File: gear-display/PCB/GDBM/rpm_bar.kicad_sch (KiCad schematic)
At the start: 7 parts, among them J4 Con_Screw_1x04_691313510004

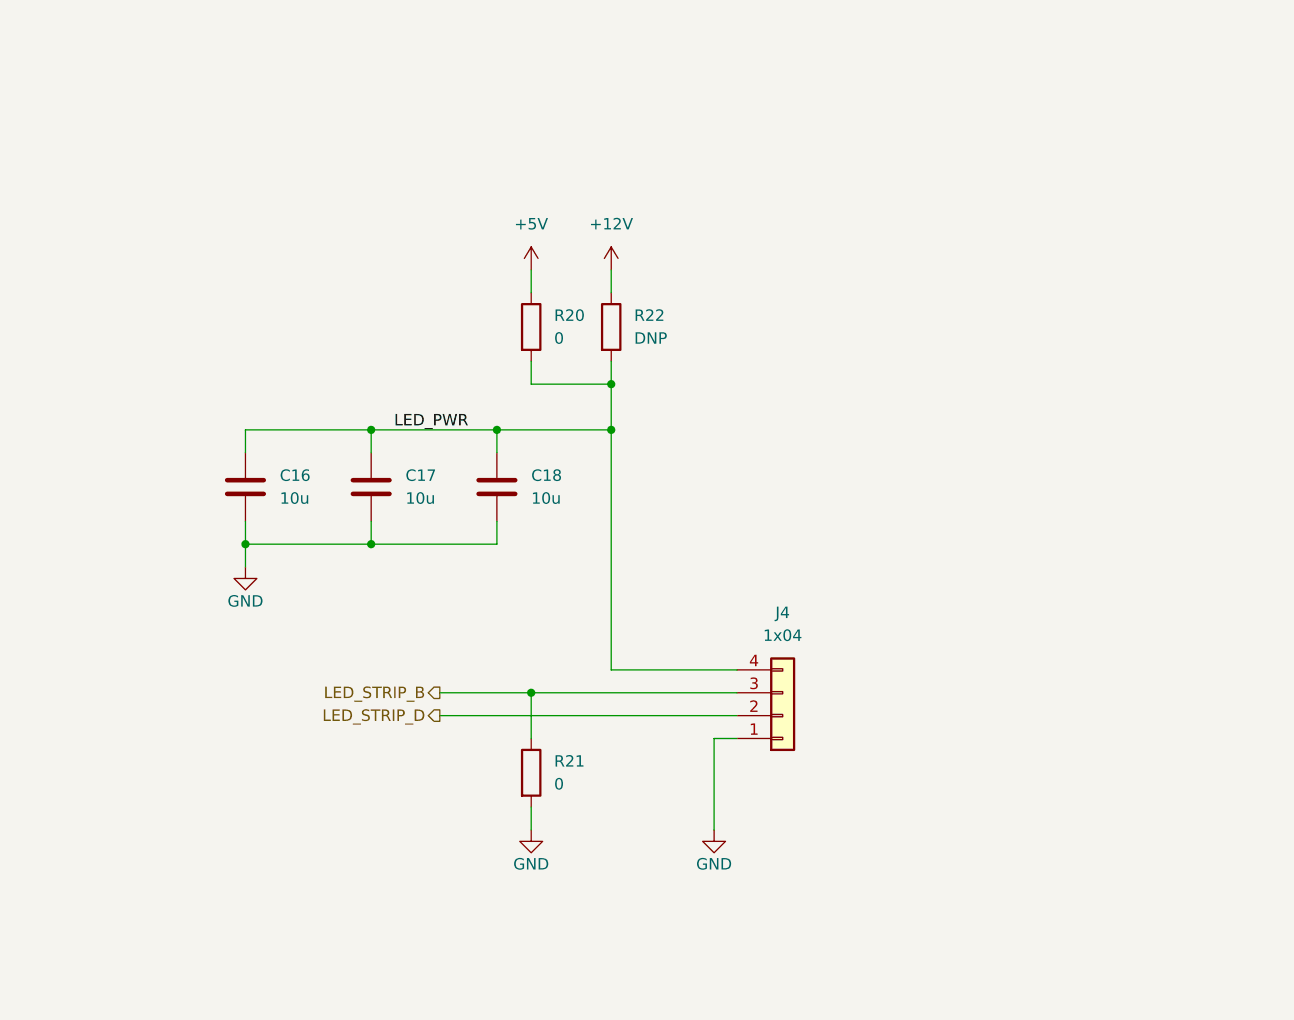
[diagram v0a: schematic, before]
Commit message: led buffer added
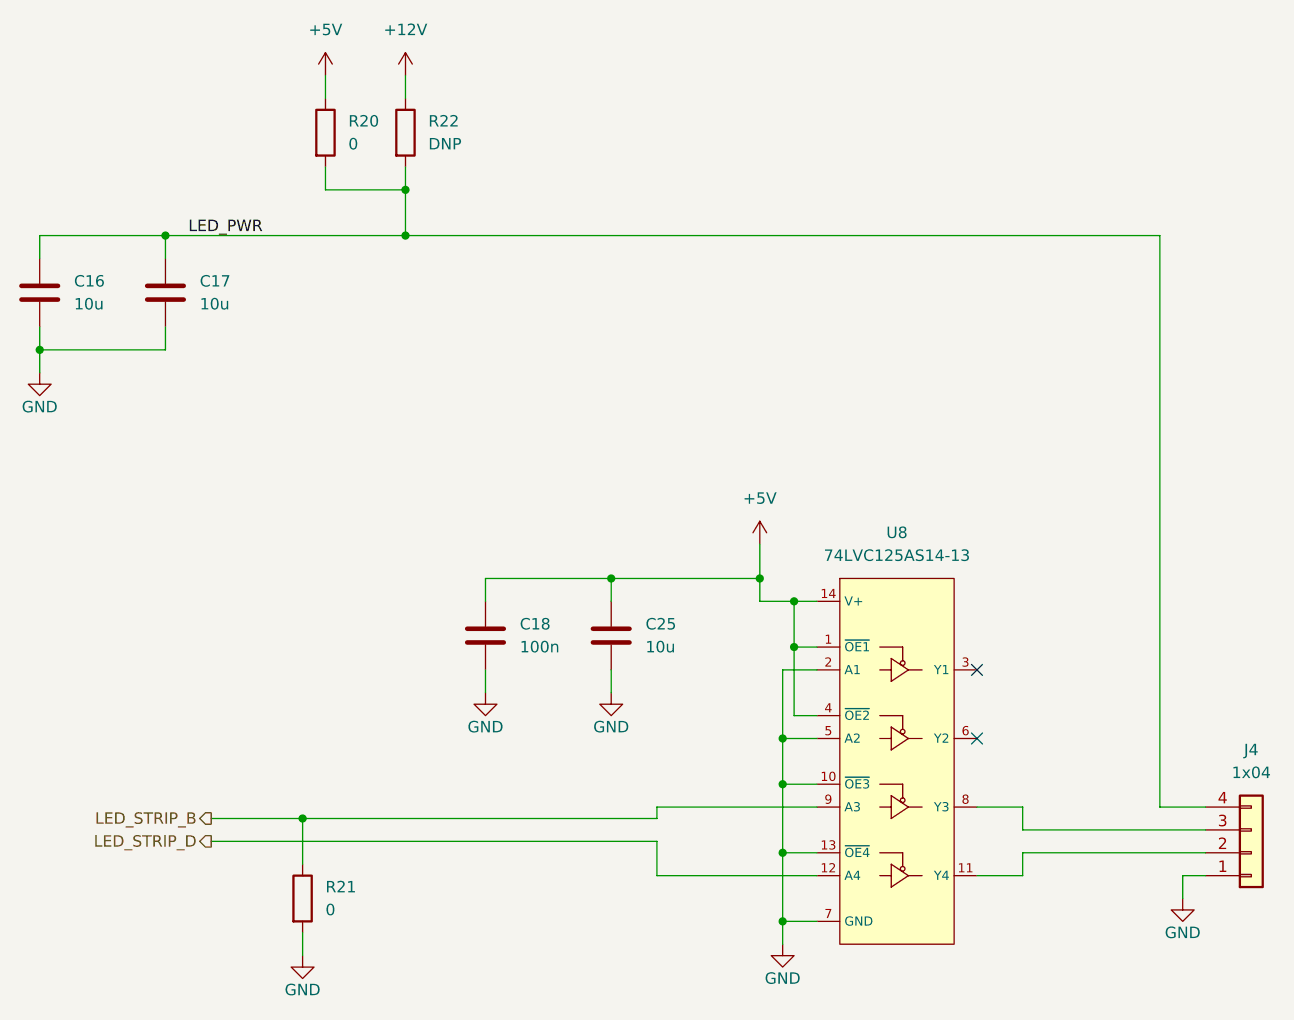
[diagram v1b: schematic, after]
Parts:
- removed C18: C_1206_10u_X5R_50V_automotive, KD_Capacitor:CAPC3216X150N, symbol KD_Capacitor:C_1206_10u_X5R_50V_automotive
- added C18: C_0603_100n_X7R_100V, KD_Capacitor:CAPC1608X90N, symbol KD_Capacitor:C_0603_100n_X7R_100V
- added C25: C_1206_10u_X5R_50V_automotive, KD_Capacitor:CAPC3216X150N, symbol KD_Capacitor:C_1206_10u_X5R_50V_automotive
- added U8: Buffer_74LVC125AS14-13_DIODES, KD_Package_SO:SOIC127P600X175-14N, symbol KD_IC_Buffer_Driver_Interface:Buffer_74LVC125AS14-13_DIODES
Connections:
- net +5V: now also C18.1, C25.1, U8.1 (~{OE1}), U8.14 (V+), U8.4 (~{OE2})
- net GND: now also C18.2, C25.2, U8.10 (~{OE3}), U8.13 (~{OE4}), U8.2 (A1), U8.5 (A2), U8.7 (GND)
- net LED_STRIP_B: now also U8.9 (A3); no longer J4.3 (Pin_3)
- net LED_STRIP_D: now also U8.12 (A4); no longer J4.2 (Pin_2)
- new net: J4.2 (Pin_2), U8.11 (Y4)
- new net: J4.3 (Pin_3), U8.8 (Y3)
- no-connect marks 0 -> 2
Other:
- moved on the sheet: C16, C17, J4, R20, R21, R22

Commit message: Layout
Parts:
- C16, C17, C25: value C_1206_10u_X5R_50V_automotive -> 10u
- C18: value C_0603_100n_X7R_100V -> 100n
- J4: value Con_Screw_1x04_691313510004 -> 1x04
- R20, R21: value R_0805_0_automotive -> 0; symbol KD_Resistor:R_0805_0_automotive -> KD_Resistor:R_0805_0
- R22: value R_0805_DNP -> DNP
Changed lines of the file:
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@@
       (effects (font (size 1.27 1.27)) (justify left))
     )
-    (property "Value" "R_0805_DNP" (at 116.84 12.7 0)
+    (property "Value" "DNP" (at 116.84 12.7 0)
       (effects (font (size 1.27 1.27)) (justify left) hide)
     )
@@
       (effects (font (size 1.27 1.27)) (justify left))
     )
-    (property "Value" "C_1206_10u_X5R_50V_automotive" (at 76.2 30.48 0)
+    (property "Value" "10u" (at 76.2 30.48 0)
       (effects (font (size 1.27 1.27)) (justify left) hide)
     )
@@
     )
   )
-  (symbol (lib_id "KD_Resistor:R_0805_0_automotive") (at 118.11 129.54 0) (unit 1)
-    (in_bom yes) (on_board yes) (dnp no) (fields_autoplaced)
-    (property "Reference" "R21" (at 120.65 128.2699 0)
-      (effects (font (size 1.27 1.27)) (justify left))
-    )
-    (property "Value" "R_0805_0_automotive" (at 105.41 97.79 0)
+  (symbol (lib_id "KD_Resistor:R_0805_0") (at 118.11 129.54 0) (unit 1)
+    (in_bom yes) (on_board yes) (dnp no) (fields_autoplaced)
+    (property "Reference" "R21" (at 120.65 128.27 0)
+      (effects (font (size 1.27 1.27)) (justify left))
+    )
+    (property "Value" "0" (at 105.41 97.79 0)
       (effects (font (size 1.27 1.27)) (justify left) hide)
     )
@@
       (effects (font (size 1.27 1.27)) (justify left) hide)
     )
-    (property "Code" "0" (at 120.65 130.8099 0)
+    (property "Code" "0" (at 120.65 130.81 0)
       (effects (font (size 1.27 1.27)) (justify left))
     )
@@
       (effects (font (size 1.27 1.27)))
     )
-    (property "Value" "Con_Screw_1x04_691313510004" (at 205.74 158.75 0)
+    (property "Value" "1x04" (at 205.74 158.75 0)
       (effects (font (size 1.27 1.27)) (justify left) hide)
     )
@@
       (effects (font (size 1.27 1.27)) (justify left))
     )
-    (property "Value" "C_1206_10u_X5R_50V_automotive" (at 139.7 68.58 0)
+    (property "Value" "10u" (at 139.7 68.58 0)
       (effects (font (size 1.27 1.27)) (justify left) hide)
     )
@@
       (effects (font (size 1.27 1.27)) (justify left))
     )
-    (property "Value" "C_0603_100n_X7R_100V" (at 125.73 68.58 0)
+    (property "Value" "100n" (at 125.73 68.58 0)
       (effects (font (size 1.27 1.27)) (justify left) hide)
     )
@@
     )
   )
-  (symbol (lib_id "KD_Resistor:R_0805_0_automotive") (at 120.65 44.45 0) (unit 1)
-    (in_bom yes) (on_board yes) (dnp no) (fields_autoplaced)
-    (property "Reference" "R20" (at 123.19 43.1799 0)
-      (effects (font (size 1.27 1.27)) (justify left))
-    )
-    (property "Value" "R_0805_0_automotive" (at 107.95 12.7 0)
+  (symbol (lib_id "KD_Resistor:R_0805_0") (at 120.65 44.45 0) (unit 1)
+    (in_bom yes) (on_board yes) (dnp no) (fields_autoplaced)
+    (property "Reference" "R20" (at 123.19 43.18 0)
+      (effects (font (size 1.27 1.27)) (justify left))
+    )
+    (property "Value" "0" (at 107.95 12.7 0)
       (effects (font (size 1.27 1.27)) (justify left) hide)
     )
@@
       (effects (font (size 1.27 1.27)) (justify left) hide)
     )
-    (property "Code" "0" (at 123.19 45.7199 0)
+    (property "Code" "0" (at 123.19 45.72 0)
       (effects (font (size 1.27 1.27)) (justify left))
     )
@@
       (effects (font (size 1.27 1.27)) (justify left))
     )
-    (property "Value" "C_1206_10u_X5R_50V_automotive" (at 90.17 30.48 0)
-      (effects (font (size 1.27 1.27)) (justify left) hide)
-    )
+    (property "Value" "10u" (at 90.17 30.48 0)
+      (effects (font (size 1.27 1.27)) (justify left) hide)
+    )
